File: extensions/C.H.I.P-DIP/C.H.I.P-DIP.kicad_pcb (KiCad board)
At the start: 2 copper layers, 4 parts, among them M1 MH_M3, M2 MH_M3, M3 MH_M3, M4 MH_M3

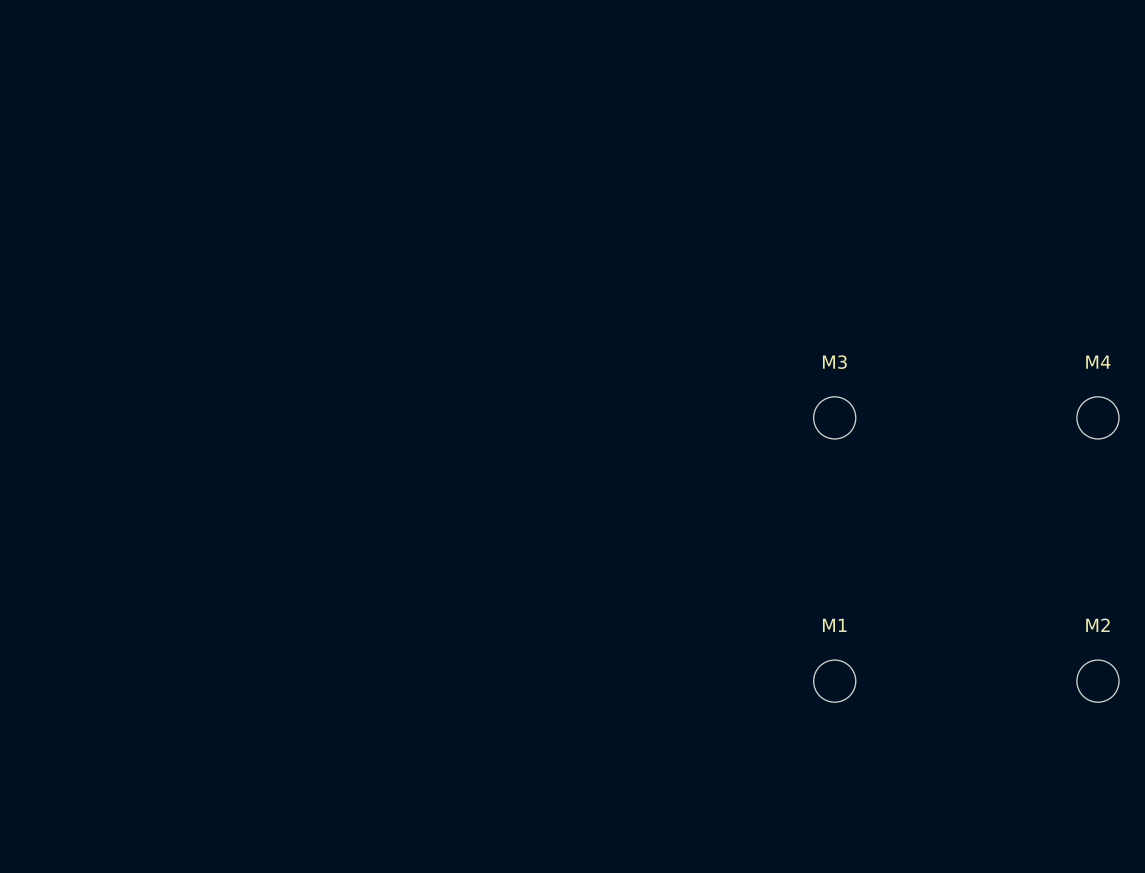
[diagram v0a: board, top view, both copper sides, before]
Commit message: Added C.H.I.P expander board
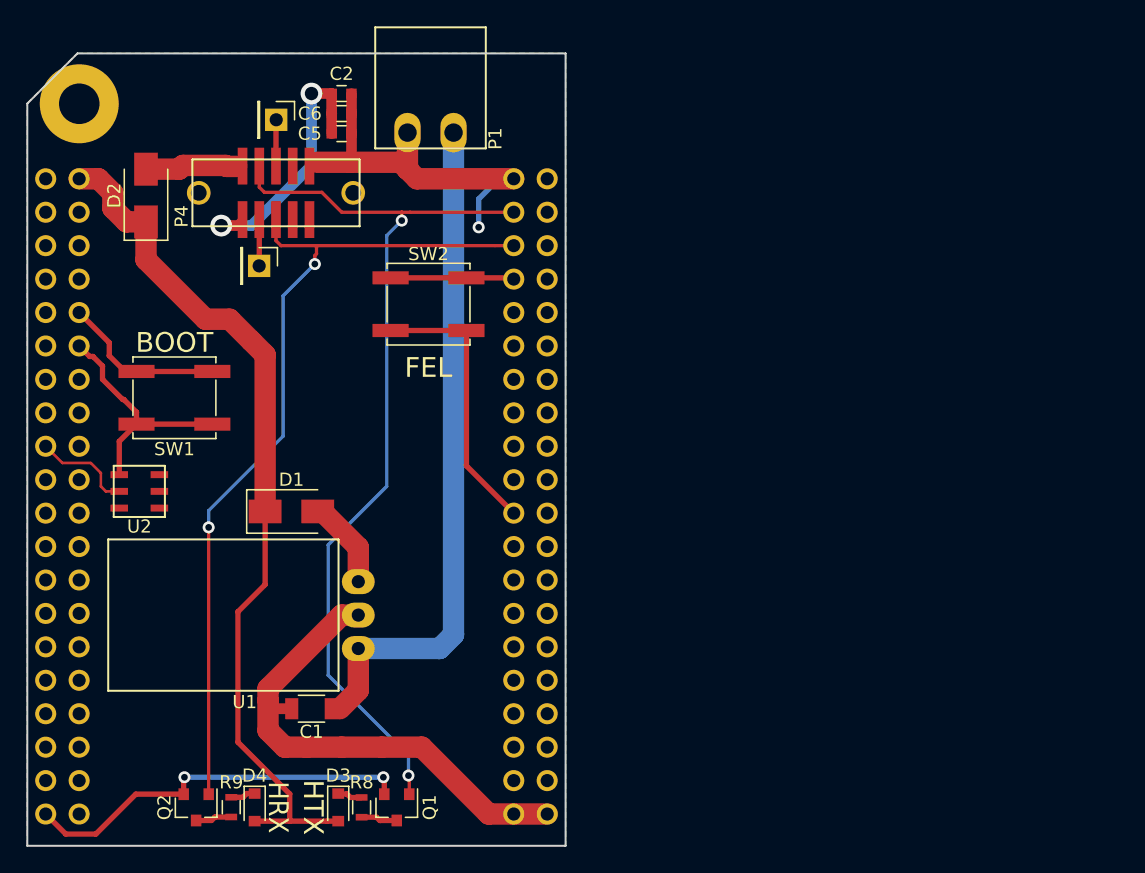
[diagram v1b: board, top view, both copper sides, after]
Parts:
- removed M1, M2, M3, M4: MH_M3, Mounting_Holes:MountingHole_3.2mm_M3
- added C1: 3.3uF/100V, Capacitors_SMD:C_1206, F.Cu at (95.2, 117.1)
- added C2: 10uF, Capacitors_SMD:C_0603, F.Cu at (97.5, 70.4)
- added C5: 1uF, Capacitors_SMD:C_0603, F.Cu at (97.5, 73.4)
- added C6: 0.1uF, Capacitors_SMD:C_0603, F.Cu at (97.5, 71.9)
- added D1: MBRA210LT3G, Diodes_SMD:D_SMA_Standard, F.Cu at (93.7, 102.1)
- added D2: MBRA210LT3G, Diodes_SMD:D_SMA_Standard, F.Cu at (82.7, 78.1)
- added D3: HTX, Diodes_SMD:D_0805, F.Cu at (97.3, 124.6)
- added D4: HRX, Diodes_SMD:D_0805, F.Cu at (90.9, 124.6)
- added P1: CONN_01X02, Smoothie-Connectors:FCI_20020110-C021A01LF, F.Cu at (104.3, 69.9)
- added P2: CONN_01X01, Pin_Headers:Pin_Header_Straight_1x01_Pitch2.54mm, F.Cu at (91.3, 83.5)
- added P3: CONN_01X01, Pin_Headers:Pin_Header_Straight_1x01_Pitch2.54mm, F.Cu at (92.6, 72.4)
- added P4: CONN_02X05, Smoothie-Connectors:SHF-105-01-L-D-SM-LC, F.Cu at (92.6, 77.9)
- added Q1: BSS214N, TO_SOT_Packages_SMD:SOT-23, F.Cu at (101.7, 124.6)
- added Q2: BSS214N, TO_SOT_Packages_SMD:SOT-23, F.Cu at (86.5, 124.6)
- added R8: 220R, Resistors_SMD:R_0603, F.Cu at (99.1, 124.6)
- added R9: 220R, Resistors_SMD:R_0603, F.Cu at (89.2, 124.6)
- added SW1: SW_PUSH, Buttons_Switches_SMD:SW_SPST_EVPBF, F.Cu at (84.8, 93.5)
- added SW2: SW_PUSH, Buttons_Switches_SMD:SW_SPST_EVPBF, F.Cu at (104.1, 86.4)
- added U1: R-78HB5.0-0.5L, Smoothie-Regulators:R-78HBx.x-x.xL, F.Cu at (98.8, 110.0)
- added U2: DS2431, Smoothie-TSOC:TSOC-6, F.Cu at (82.2, 100.6)
- added U3: C.H.I.P, C.H.I.P:C.H.I.P, F.Cu at (94.1, 99.7)
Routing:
- net GND: track 0.00 -> 137.9 mm, vias 0 -> 3
- net /HTXSRX: track 0.00 -> 70.8 mm, vias 0 -> 2
- net +5V: track 0.00 -> 66.3 mm
- net /HRXSTX: track 0.00 -> 64.9 mm, vias 0 -> 2
- net Net-(C1-Pad1): track 0.00 -> 51.6 mm
- net +3V3: track 0.00 -> 20.6 mm, vias 0 -> 2
- net Net-(SW1-Pad2): track 0.00 -> 12.6 mm
- net Net-(SW2-Pad2): track 0.00 -> 9.40 mm
- net Net-(U2-Pad2): track 0.00 -> 7.60 mm
- net Net-(D2-Pad2): track 0.00 -> 7.50 mm
- net Net-(D1-Pad2): track 0.00 -> 6.81 mm
- net Net-(P3-Pad1): track 0.00 -> 3.55 mm
- net Net-(P2-Pad1): track 0.00 -> 3.52 mm
- net Net-(Q2-Pad3): track 0.00 -> 2.78 mm
- net Net-(Q1-Pad3): track 0.00 -> 2.77 mm
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- added copper zone on B.Cu, net GND
- added copper zone on F.Cu, net GND
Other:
- board outline added: 40.9 x 60.2 mm
- net class Default: clearance 0.2 -> 0.2032; trace_width 0.25 -> 0.2032; via_dia 0.6 -> 0.7366; via_drill 0.4 -> 0.3302
- rule trace_clearance: 0.2 -> 0.2032
- board text added: "BOOT"
- board text added: "FEL"
- board text added: "HRX"
- board text added: "HTX"
